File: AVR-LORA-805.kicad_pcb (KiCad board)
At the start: 2 copper layers, 51.7 x 29.2 mm, 36 parts, among them J1 Batt, J2 Solar, J3 SMA, J4 CONN_01X14, J5 CONN_01X14, U1 MCP1700-3302E_SOT23, U2 RFM95HW, U3 AVR128DB28, Y1 24MHz, Y2 32768Hz

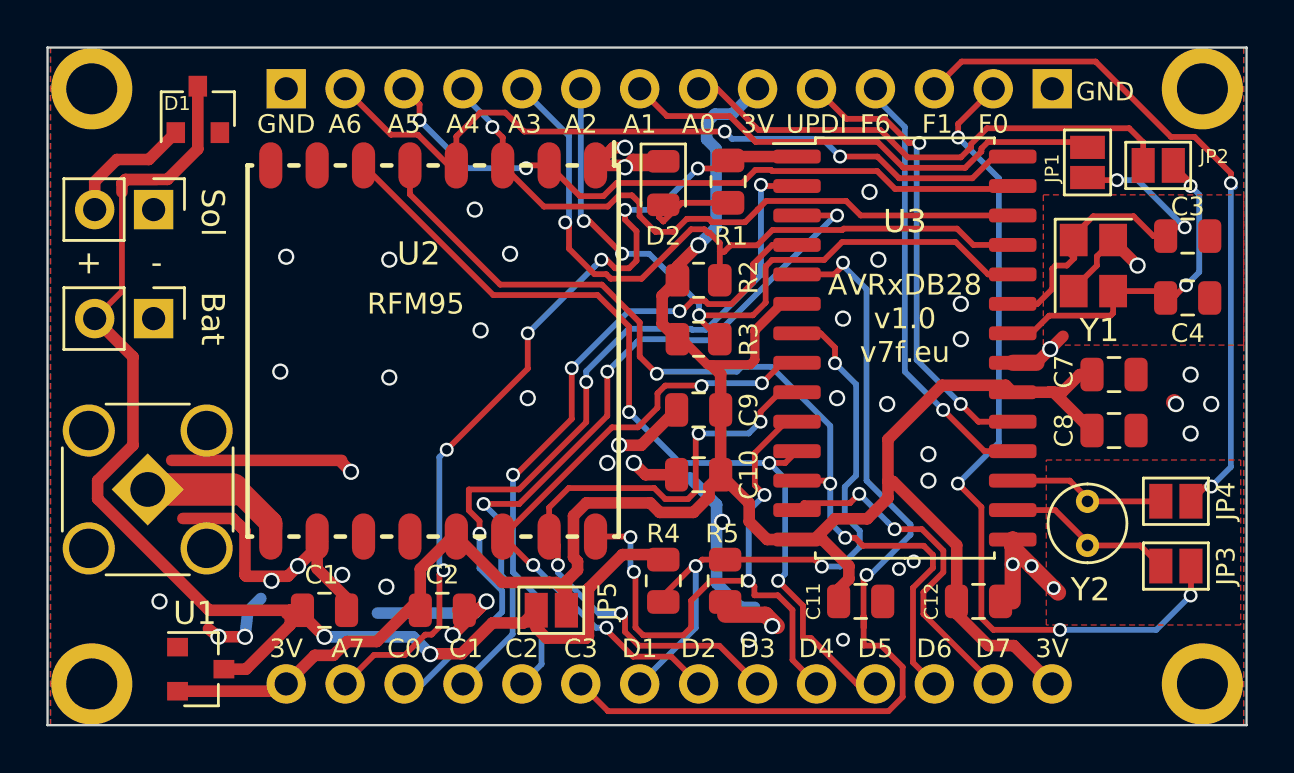
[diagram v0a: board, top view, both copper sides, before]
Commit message: Improve routes 805
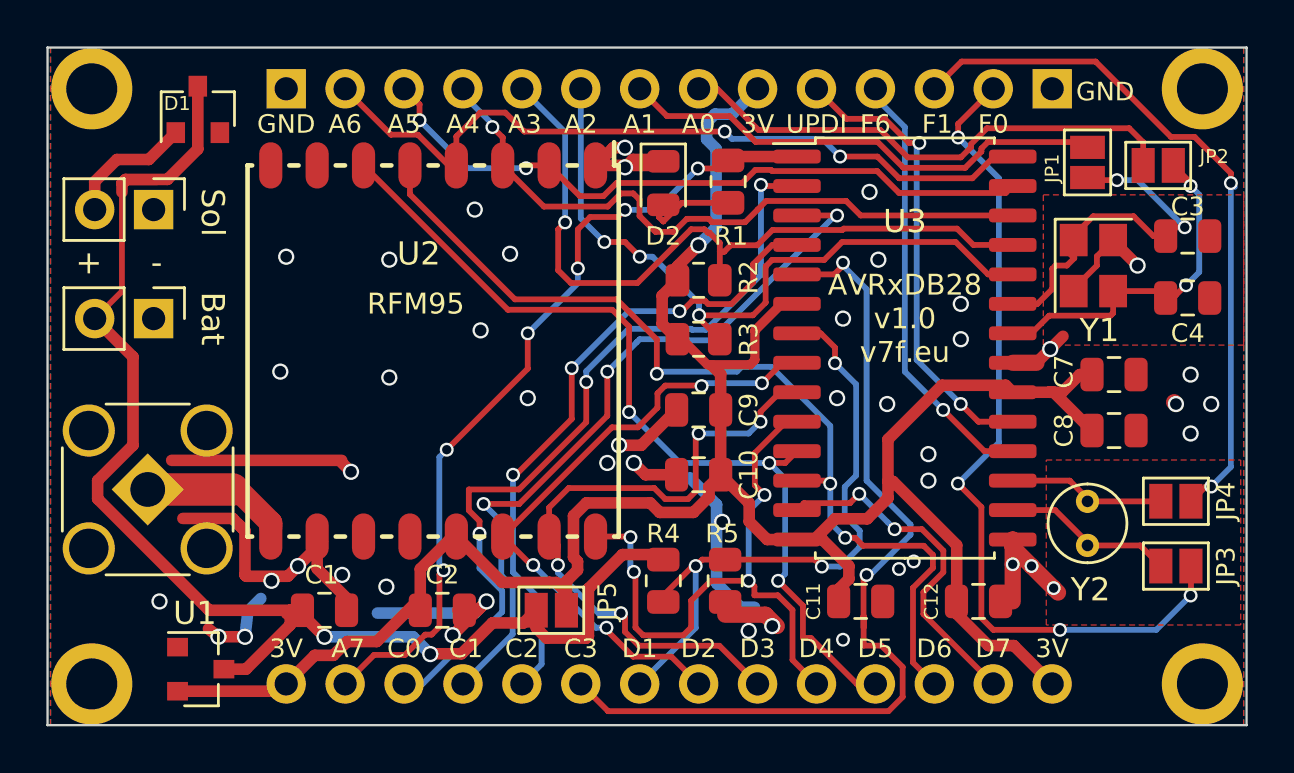
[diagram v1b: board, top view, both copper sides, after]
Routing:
- net /A3: track 31.1 -> 32.2 mm
- net /A7: track 36.5 -> 35.6 mm

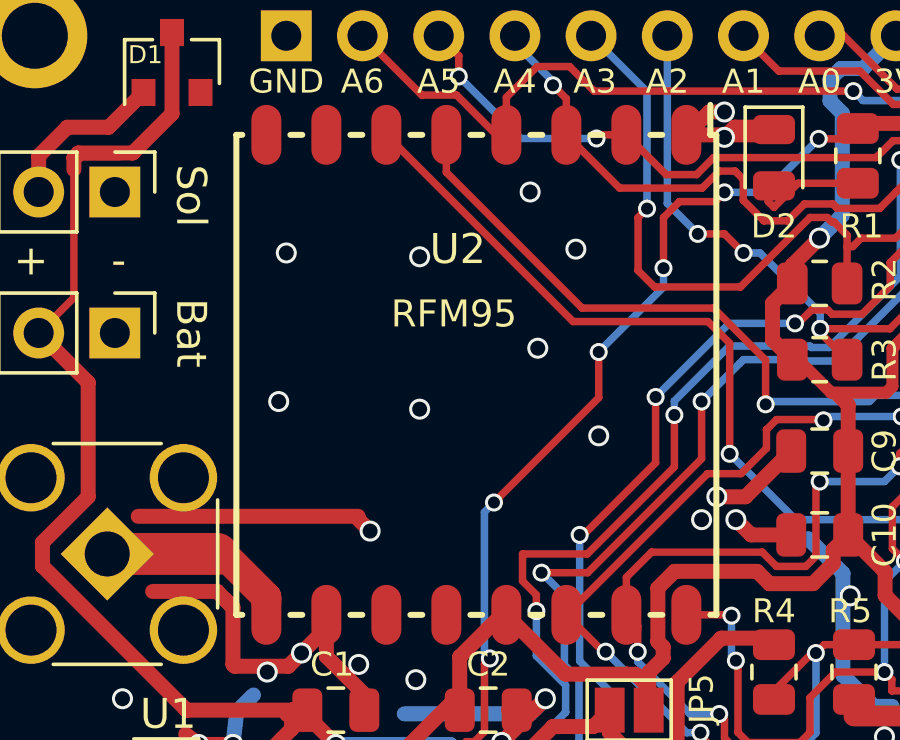
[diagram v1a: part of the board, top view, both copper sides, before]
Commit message: Add KiCAD logo
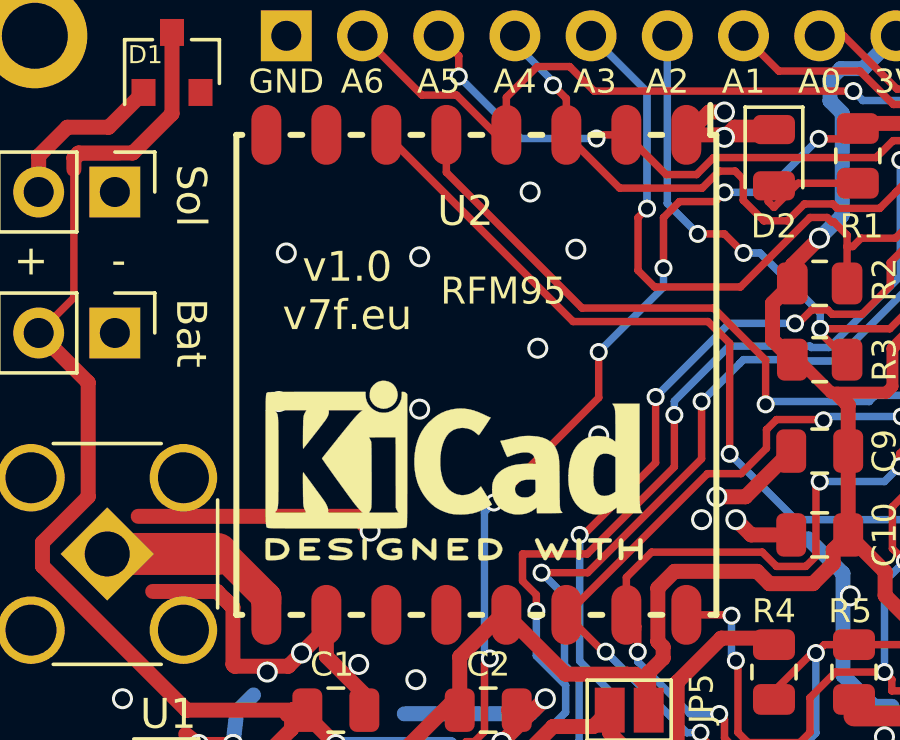
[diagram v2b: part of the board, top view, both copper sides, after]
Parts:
- added REF**: KiCad-Logo2_5mm_SilkScreen, Symbol:KiCad-Logo2_5mm_SilkScreen, F.Cu at (83.6, 97.9)
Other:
- board text added: "v1.0 v7f.eu"

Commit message: Add KiCAD logo
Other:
- board text removed: "v1.0 v7f.eu"

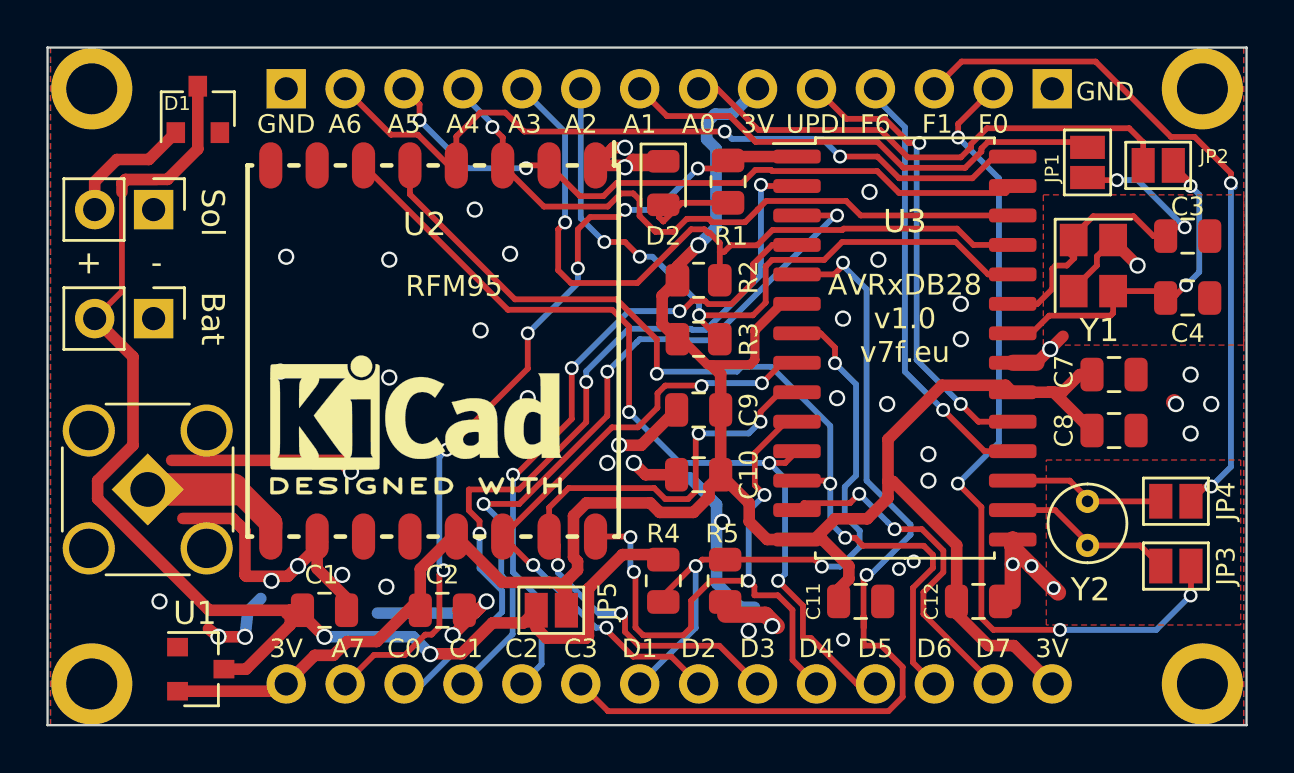
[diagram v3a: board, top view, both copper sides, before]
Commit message: Add capacitors to 32768 crystal for 0805 version
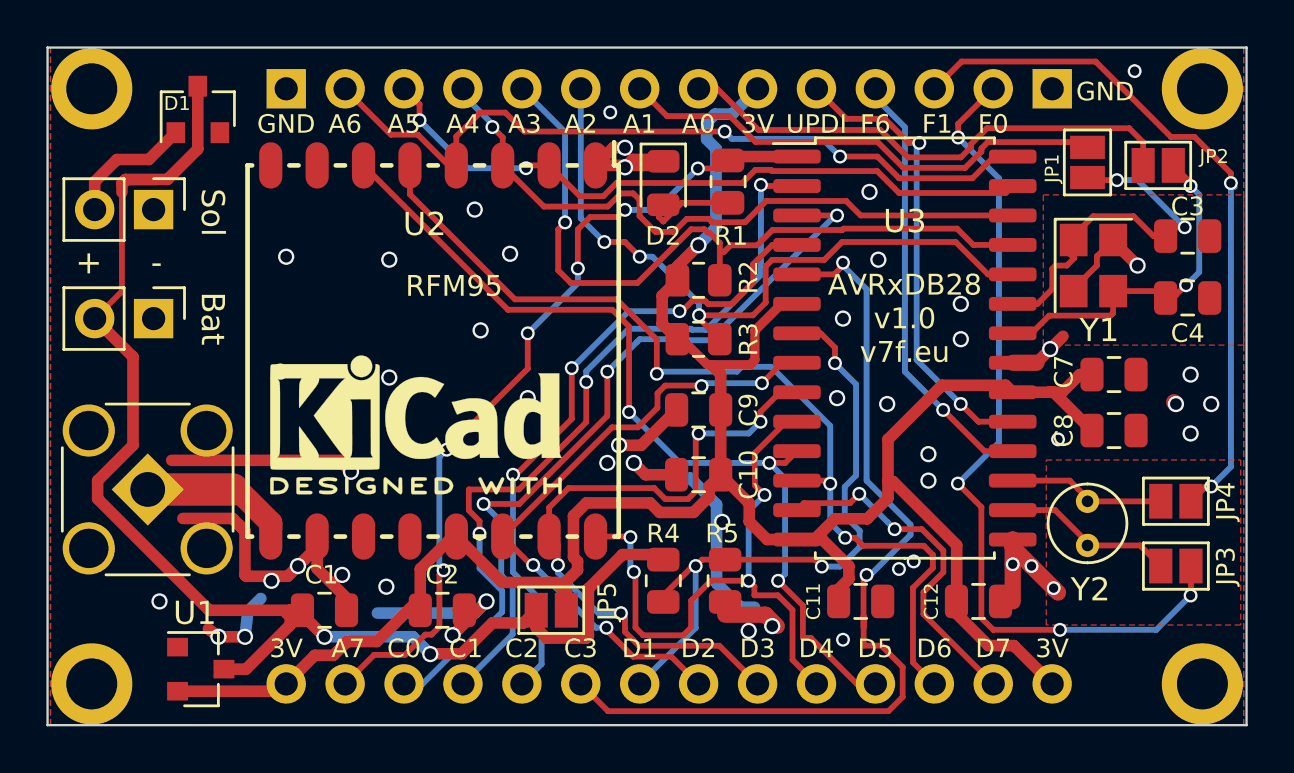
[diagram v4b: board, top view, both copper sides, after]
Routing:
- net GND: vias 47 -> 50

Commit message: Add capacitors to 32768 crystal for both versions
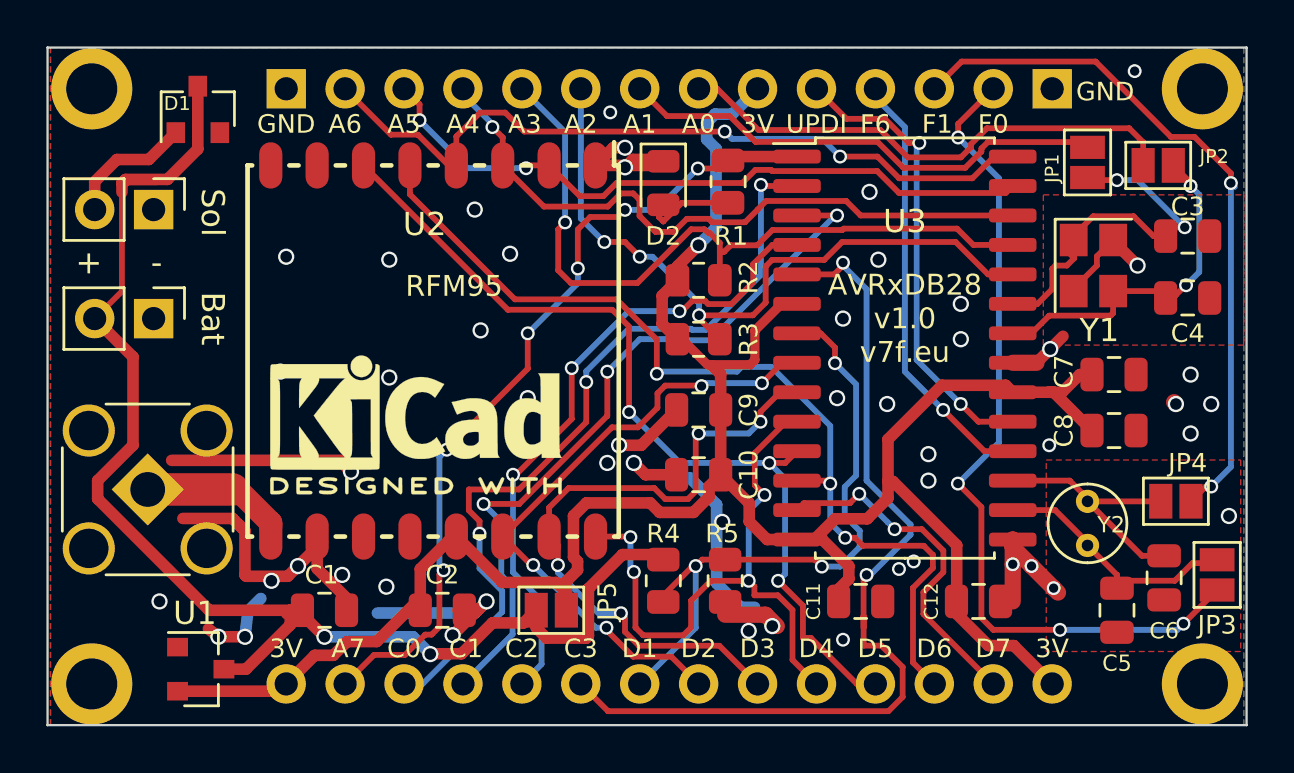
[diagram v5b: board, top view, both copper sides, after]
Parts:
- added C5: 10pF, Capacitor_SMD:C_0805_2012Metric, F.Cu at (113.8, 105.9)
- added C6: 10pF, Capacitor_SMD:C_0805_2012Metric, F.Cu at (115.8, 104.5)
- moved JP3 1.82 mm to (118.1, 104.4), turned to 270 degrees
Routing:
- net /F1: track 6.88 -> 11.2 mm
- net /F0: track 7.51 -> 11.3 mm
- net GND: vias 50 -> 51

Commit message: 1.1 version
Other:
- board text added: "AVRxDB28 v1.1 v7f.eu"
- board text removed: "AVRxDB28 v1.0 v7f.eu"

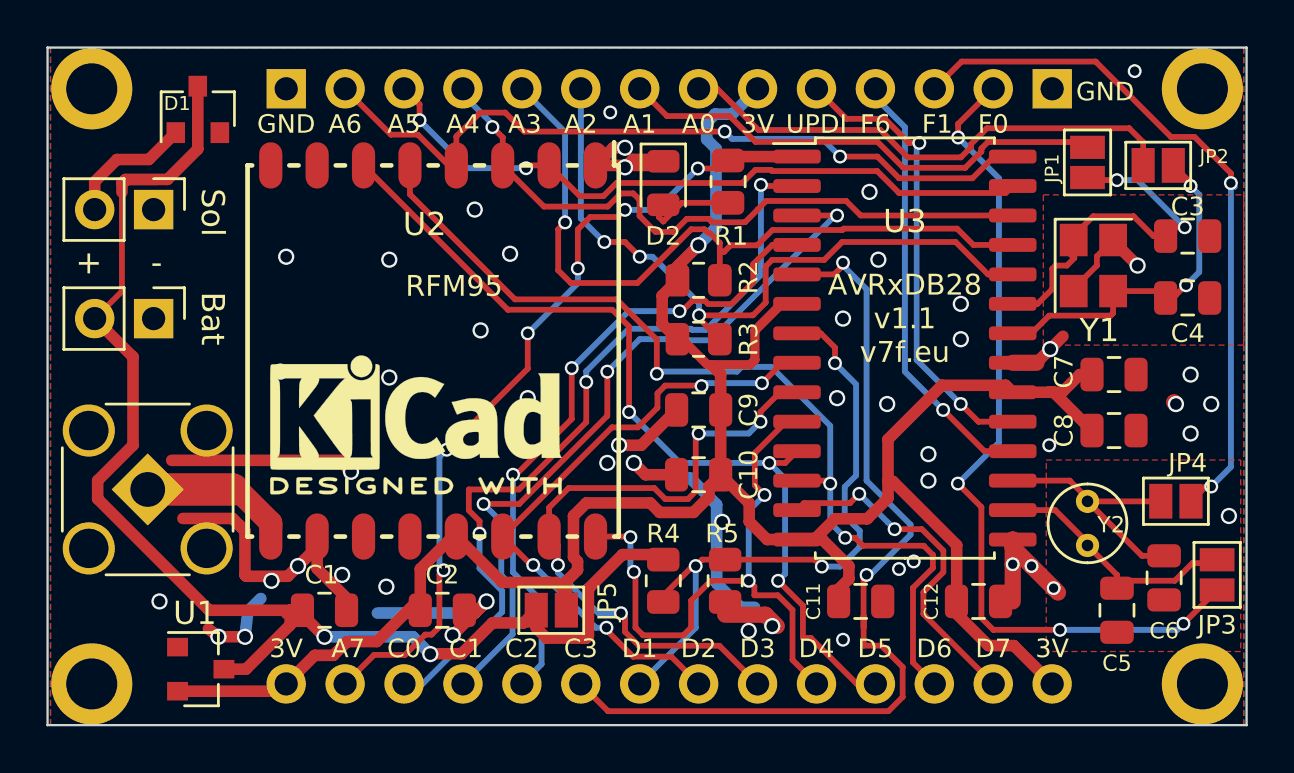
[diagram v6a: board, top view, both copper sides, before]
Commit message: Silk and routing improvements
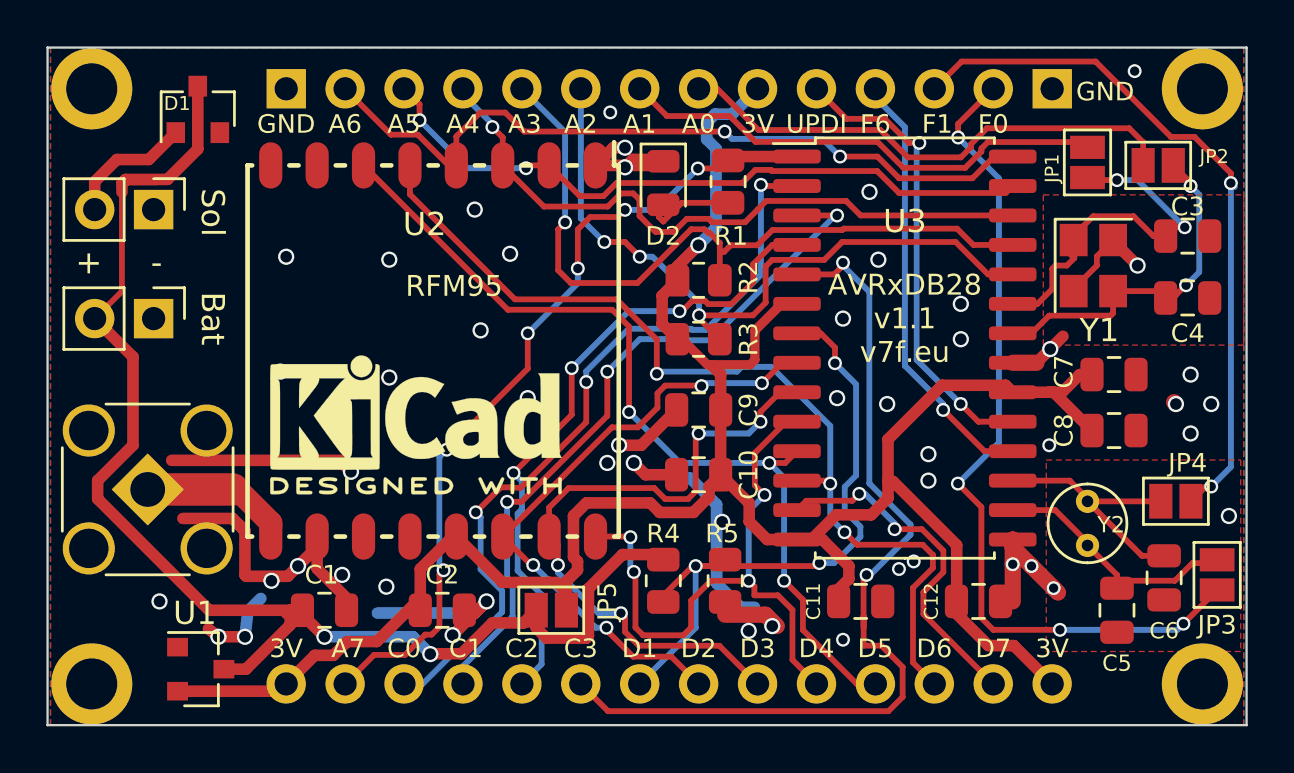
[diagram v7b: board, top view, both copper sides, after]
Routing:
- net /C1: track 32.7 -> 31.3 mm
- net /C0: track 34.6 -> 33.6 mm
- net /D1: track 27.3 -> 28.2 mm

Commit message: crystal grounding
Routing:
- net GND: track 68.5 -> 71.2 mm, vias 51 -> 55
- net /CF0: track 36.4 -> 37.3 mm
